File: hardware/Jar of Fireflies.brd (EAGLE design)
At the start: 81.3 x 81.3 mm, 17 parts, among them IC1 ATTINY85, J1 POWER_JACKPTH, J3 M022.54MM_SCREWTERM

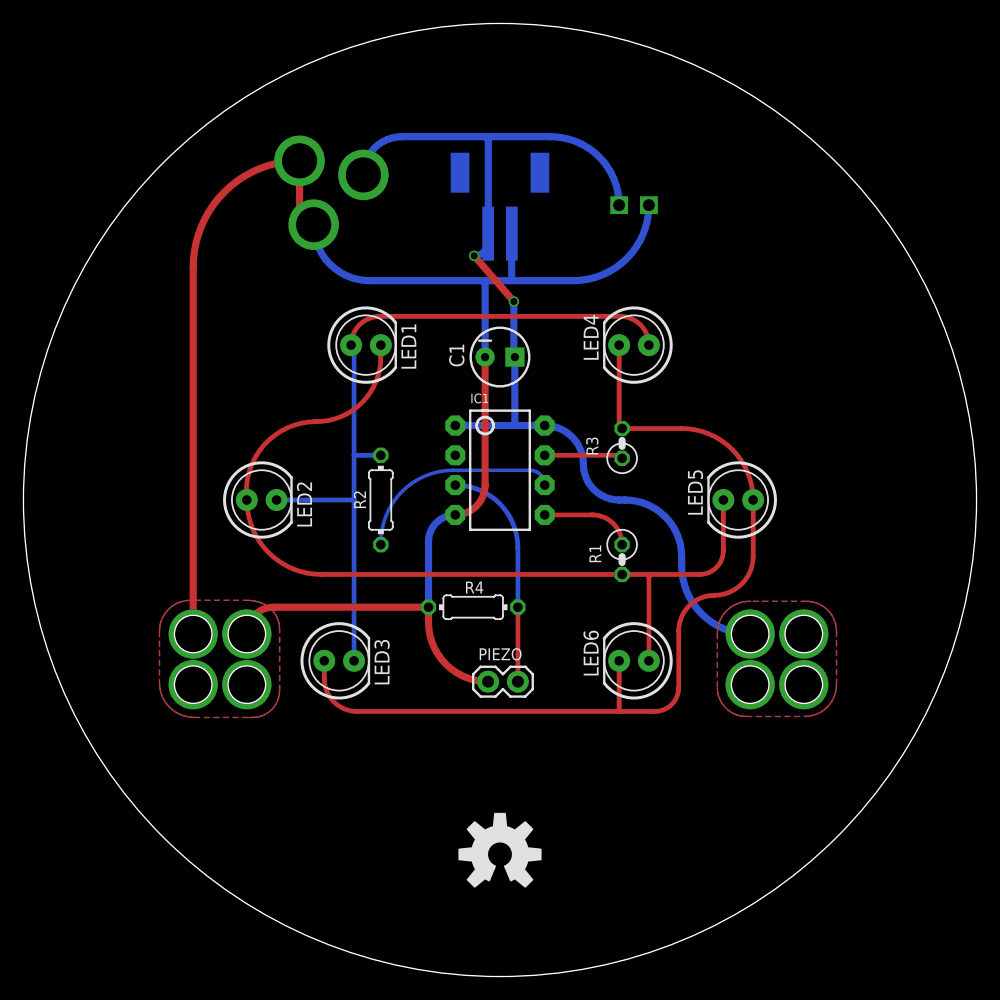
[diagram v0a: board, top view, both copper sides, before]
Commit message: Updating PCB design with ICSP, SMD pads for LEDs, sensor interface, and different power options
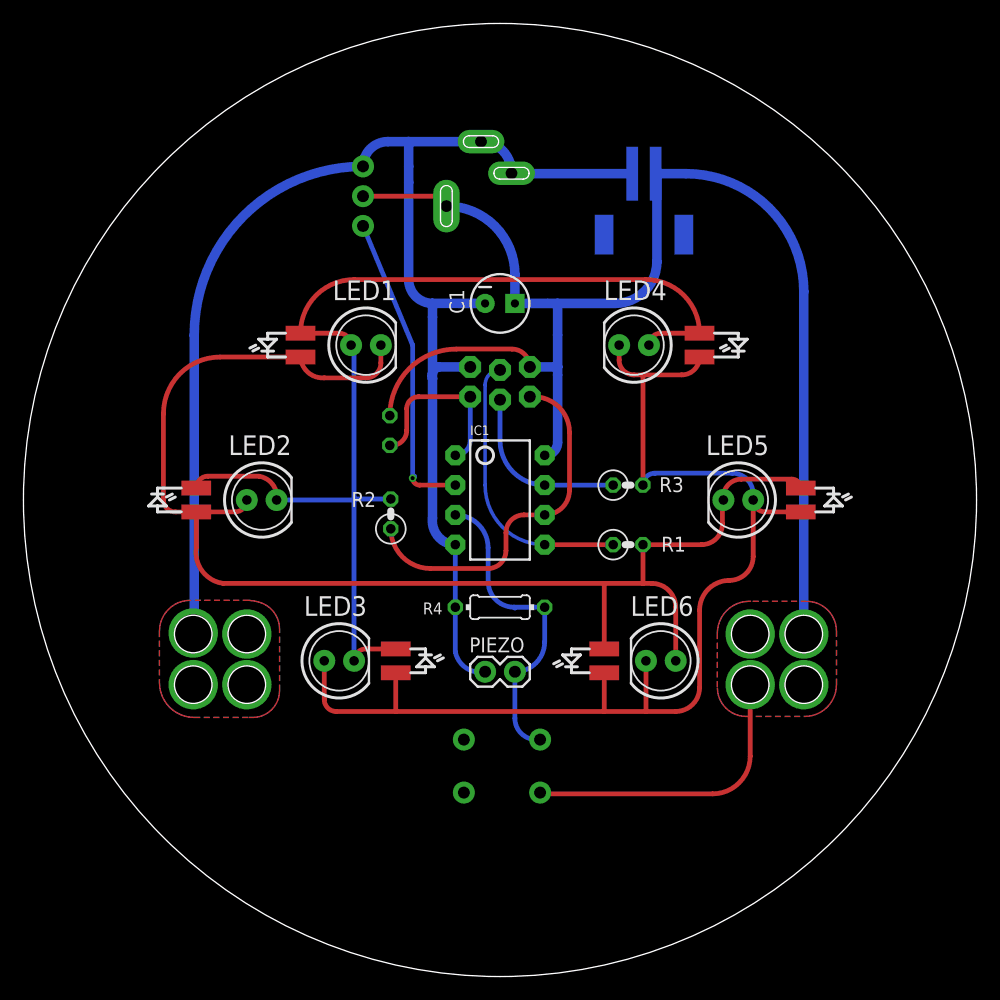
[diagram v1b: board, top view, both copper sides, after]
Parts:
- removed LOGO1: OSHW-LOGOL, SparkFun-Aesthetics:OSHW-LOGO-L
- added J4: ICSP, SparkFun-Connectors:2X3_LOCK
- added PAD1, PAD10, PAD11, PAD12, PAD2, PAD3, PAD4, PAD5, PAD6, PAD7, PAD8, PAD9: (no value), wirepad:SMD1,27-2,54
- added R5: 10k, resistor:0207/2V
- added S1: (no value), SparkFun-Electromechanical:TACTILE-PTH
- J1: value POWER_JACKPTH -> PJ-006A; device SparkFun-Connectors:POWER_JACK_PTH -> PJ-006A:CUI_PJ-006A
- J2: value (none) -> JST
- J3: value M022.54MM_SCREWTERM -> SENSOR; device SparkFun-Connectors:1X02_2.54_SCREWTERM -> SparkFun-Connectors:1X03
- R1, R3: value 150 -> (none)
- R2: value 150 -> (none); device resistor:0204/7 -> resistor:0207/2V
- moved J3 24.4 mm to (29.0, 64.0), turned to 90 degrees
- moved J1 18.2 mm to (36.1, 65.7), turned to 270 degrees
- moved J2 12.5 mm to (52.9, 64.8), turned to 180 degrees
- moved C1 4.57 mm to (40.6, 57.4)
- moved R3 3.59 mm to (51.6, 41.9), turned to 0 degrees
- moved IC1 2.54 mm to (40.6, 40.6)
- moved LED6 2.29 mm to (54.4, 26.9)
- moved R4 2.29 mm to (40.6, 31.5)
- moved R2 1.46 mm to (31.3, 39.5)
- moved R1 1.37 mm to (51.6, 36.8), turned to 0 degrees
- moved PIEZO 0.88 mm to (39.4, 26.0)
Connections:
- removed net N$1: LED1.A, LED2.K, LED3.K, LED4.A, R2.2
- removed net N$3: LED3.A, LED4.K, LED5.A, LED6.K, R3.2
- removed net PORTA: IC1.5, R1.1
- removed net PORTB: IC1.6, R2.1
- removed net PORTC: IC1.7, R3.1
- new net A: LED1.K, LED2.A, LED5.K, LED6.A, PAD1.1, PAD11.1, PAD5.1, PAD9.1, R1.2
- new net B: LED1.A, LED2.K, LED3.K, LED4.A, PAD2.1, PAD3.1, PAD6.1, PAD7.1, R2.2
- new net C: LED3.A, LED4.K, LED5.A, LED6.K, PAD10.1, PAD12.1, PAD4.1, PAD8.1, R3.2
- new net MISO: IC1.6, J4.1, R2.1
- new net MOSI: IC1.5, J4.4, R1.1
- new net RESET: IC1.1, J4.5, R5.1
- new net SCK: IC1.7, J4.3, R3.1
- new net SENSOR: IC1.2, J3.1
- net GND: now also J1.2, J1.3, J3.3, J4.6; no longer J1.GND, J1.GNDBREAK, J3.P2
- net N$2: now also PIEZO.2, R4.2, S1.1; no longer LED1.K, LED2.A, LED5.K, LED6.A, R1.2
- net PIEZO: no longer PIEZO.2, R4.2
- net VCC: now also J1.1, J3.2, J4.2, R5.2, S1.3; no longer IC1.1, J1.PWR, J3.P1
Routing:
- net A: track 0.00 -> 115.7 mm
- net C: track 0.00 -> 99.6 mm
- net B: track 0.00 -> 96.3 mm
- net N$3: track 77.6 -> 0.00 mm
- net N$1: track 63.3 -> 0.00 mm
- net N$2: track 73.6 -> 13.4 mm
- net VCC: track 85.6 -> 141.4 mm, vias 6 -> 4
- net MISO: track 0.00 -> 29.9 mm
- net SENSOR: track 0.00 -> 26.5 mm, vias 0 -> 1
- net MOSI: track 0.00 -> 23.4 mm
- net PORTB: track 17.2 -> 0.00 mm
- net RESET: track 0.00 -> 15.2 mm
- net GND: track 142.2 -> 127.3 mm
- net SCK: track 0.00 -> 14.7 mm
- net PORTA: track 7.66 -> 0.00 mm
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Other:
- board text added: "S"
- board text added: "Silkscreen artwork is on layer 200"
- board text removed: "OSHW"
- board text removed: "REV B"

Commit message: Switching to vertical JST jack
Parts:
- J2: value JST -> (none); device SparkFun-Connectors:JST-2-SMD -> SparkFun-Connectors:JST-2-PTH-VERT
- moved J2 2.19 mm to (51.6, 66.6), turned to 270 degrees
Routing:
- net VCC: track 141.4 -> 129.6 mm, vias 4 -> 5
- net SENSOR: track 26.5 -> 27.4 mm
- net GND: track 127.3 -> 128.1 mm
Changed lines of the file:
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@@
 <attribute name="NAME" x="54.22064375" y="41.317240625" size="1.27" layer="25" font="vector" ratio="12"/>
-</element>
-<element name="J2" library="SparkFun-Connectors" package="JST-2-SMD" value="JST" x="52.916734375" y="64.769975" smashed="yes" rot="MR180">
-<attribute name="PROD_ID" value="CONN-08352" x="52.916734375" y="64.769975" size="1.778" layer="28" rot="MR180" display="off"/>
 </element>
 <element name="C1" library="SparkFun-Capacitors" package="CPOL-RADIAL-10UF-25V" value="10uF" x="40.64" y="57.404353125" smashed="yes">
@@
 <attribute name="STANDARD" value="Manufacturer recommendations" x="36.069803125" y="65.704625" size="1.778" layer="28" rot="MR270" display="off"/>
 </element>
+<element name="J2" library="SparkFun-Connectors" package="JST-2-PTH-VERT" value="" x="51.64924375" y="66.551328125" rot="MR270"/>
 </elements>
 <signals>
@@
 <contactref element="PIEZO" pad="1"/>
 <contactref element="R4" pad="1"/>
-<contactref element="J2" pad="1"/>
 <contactref element="C1" pad="2"/>
 <via x="19.05" y="29.21" extent="1-16" drill="3.2"/>
@@
 <wire x1="41.619803125" y1="68.604625" x2="41.619803125" y2="68.504625" width="0.8128" layer="16"/>
 <wire x1="41.619803125" y1="68.504625" x2="41.654453125" y2="68.469975" width="0.8128" layer="16" curve="90"/>
-<wire x1="41.654453125" y1="68.469975" x2="51.916734375" y2="68.469975" width="0.8128" layer="16"/>
 <wire x1="32.852309375" y1="69.091453125" x2="32.852309375" y2="69.091453125" width="0.8128" layer="16" curve="90"/>
 <wire x1="32.852309375" y1="69.091453125" x2="32.852309375" y2="67.73671875" width="0.8128" layer="16"/>
@@
 <wire x1="14.56339375" y1="54.69715" x2="28.95745" y2="69.09120625" width="0.8128" layer="16" curve="-90"/>
 <wire x1="14.56339375" y1="29.38028125" x2="14.56339375" y2="54.69715" width="0.8128" layer="16"/>
+<contactref element="J2" pad="1"/>
+<wire x1="41.619803125" y1="68.504625" x2="51.245946875" y2="68.504625" width="0.8128" layer="16"/>
+<wire x1="51.245946875" y1="68.504625" x2="52.19924375" y2="67.551328125" width="0.8128" layer="16" curve="-90"/>
 </signal>
 <signal name="MISO">
@@
 <signal name="VCC">
 <contactref element="IC1" pad="8"/>
-<contactref element="J2" pad="2"/>
 <contactref element="C1" pad="1"/>
 <via x="61.976" y="29.21" extent="1-16" drill="3.2"/>
-<via x="66.548" y="29.21" extent="1-16" drill="3.2"/>
 <via x="66.548" y="24.892" extent="1-16" drill="3.2"/>
 <via x="61.976" y="24.892" extent="1-16" drill="3.2"/>
@@
 <vertex x="61.631171875" y="22.180446875"/>
 </polygon>
-<wire x1="66.548" y1="58.42" x2="66.548" y2="29.21" width="0.8128" layer="16"/>
 <contactref element="S1" pad="3"/>
-<wire x1="53.916734375" y1="68.469975" x2="56.498025" y2="68.469975" width="0.8128" layer="16"/>
-<wire x1="56.498025" y1="68.469975" x2="66.548" y2="58.42" width="0.8128" layer="16" curve="-90"/>
 <wire x1="61.976" y1="24.892" x2="61.976" y2="18.79384375" width="0.4064" layer="1"/>
 <wire x1="61.976" y1="18.79384375" x2="58.761603125" y2="15.579446875" width="0.4064" layer="1" curve="-90"/>
@@
 <wire x1="44.1698375" y1="15.579446875" x2="44.060540625" y2="15.68874375" width="0.4064" layer="1" curve="-90"/>
 <contactref element="J4" pad="2"/>
-<wire x1="44.45" y1="44.45" x2="45.55294375" y2="45.55294375" width="0.8128" layer="16" curve="90"/>
-<wire x1="45.55294375" y1="54.69694375" x2="45.55294375" y2="51.98793125" width="0.8128" layer="16"/>
-<wire x1="45.55294375" y1="51.310565625" x2="45.55294375" y2="45.55294375" width="0.8128" layer="16"/>
 <wire x1="43.182290625" y1="51.9878" x2="43.182421875" y2="51.98793125" width="0.8128" layer="16" curve="-90"/>
 <contactref element="R5" pad="2"/>
@@
 <wire x1="36.91501875" y1="53.512009375" x2="41.657953125" y2="53.512009375" width="0.4064" layer="1"/>
 <wire x1="41.657953125" y1="53.512009375" x2="43.182159375" y2="51.987803125" width="0.4064" layer="1" curve="-90"/>
-<wire x1="41.91" y1="57.404353125" x2="44.706234375" y2="57.404353125" width="0.8128" layer="16"/>
-<wire x1="44.706234375" y1="57.404353125" x2="45.55294375" y2="57.404353125" width="0.8128" layer="16"/>
-<wire x1="45.55294375" y1="57.404353125" x2="45.55294375" y2="54.69694375" width="0.8128" layer="16"/>
 <contactref element="J1" pad="1"/>
-<wire x1="45.55294375" y1="51.98793125" x2="45.55294375" y2="51.310565625" width="0.8128" layer="16"/>
-<wire x1="43.182159375" y1="51.987803125" x2="45.552815625" y2="51.987803125" width="0.8128" layer="16"/>
-<wire x1="45.552815625" y1="51.987803125" x2="45.55294375" y2="51.98793125" width="0.8128" layer="16"/>
-<wire x1="45.55294375" y1="57.404353125" x2="50.461340625" y2="57.404353125" width="0.8128" layer="16"/>
-<wire x1="50.461340625" y1="57.404353125" x2="54.020034375" y2="60.963046875" width="0.8128" layer="16" curve="90"/>
-<wire x1="54.020034375" y1="60.963046875" x2="54.020034375" y2="68.366675" width="0.8128" layer="16"/>
-<wire x1="54.020034375" y1="68.366675" x2="53.916734375" y2="68.469975" width="0.8128" layer="16" curve="90"/>
 <contactref element="J3" pad="2"/>
-<wire x1="36.069803125" y1="65.704625" x2="41.91" y2="59.864428125" width="0.8128" layer="16" curve="-90"/>
-<wire x1="41.91" y1="59.864428125" x2="41.91" y2="57.404353125" width="0.8128" layer="16"/>
 <wire x1="28.95745" y1="66.55120625" x2="35.223221875" y2="66.55120625" width="0.4064" layer="1"/>
 <wire x1="35.223221875" y1="66.55120625" x2="36.069803125" y2="65.704625" width="0.4064" layer="1" curve="-90"/>
+<contactref element="J2" pad="2"/>
+<via x="66.548228125" y="29.21" extent="1-16" drill="3.2"/>
+<wire x1="66.548228125" y1="29.21" x2="66.548228125" y2="48.916953125" width="0.8128" layer="16"/>
+<wire x1="36.069803125" y1="65.704625" x2="41.65808125" y2="65.704625" width="0.8128" layer="16"/>
+<wire x1="41.91" y1="57.404353125" x2="41.91" y2="65.45270625" width="0.8128" layer="16"/>
+<wire x1="41.91" y1="65.45270625" x2="41.65808125" y2="65.704625" width="0.8128" layer="16" curve="90"/>
+<wire x1="43.182159375" y1="51.987803125" x2="43.182159375" y2="56.13219375" width="0.8128" layer="16"/>
+<wire x1="43.182159375" y1="56.13219375" x2="41.91" y2="57.404353125" width="0.8128" layer="16" curve="90"/>
+<wire x1="44.45" y1="44.45" x2="45.55294375" y2="45.55294375" width="0.8128" layer="16" curve="90"/>
+<wire x1="45.55294375" y1="49.61701875" x2="43.182159375" y2="51.987803125" width="0.8128" layer="16" curve="90"/>
+<wire x1="45.55294375" y1="45.55294375" x2="45.55294375" y2="49.61701875" width="0.8128" layer="16"/>
+<via x="66.548228125" y="48.916953125" extent="1-16" drill="0.35"/>
+<wire x1="41.65808125" y1="65.704625" x2="52.045946875" y2="65.704625" width="0.8128" layer="16"/>
+<wire x1="52.045946875" y1="65.704625" x2="52.19924375" y2="65.551328125" width="0.8128" layer="16" curve="-90"/>
+<wire x1="66.548228125" y1="48.916953125" x2="66.548228125" y2="51.20234375" width="0.8128" layer="16"/>
+<wire x1="66.548228125" y1="51.20234375" x2="52.19924375" y2="65.551328125" width="0.8128" layer="16" curve="90"/>
 <wire x1="43.182159375" y1="51.987803125" x2="43.182290625" y2="51.9878" width="0" layer="19" extent="16-16"/>
 </signal>
@@
 <wire x1="33.785784375" y1="41.91" x2="33.19099375" y2="42.504790625" width="0.4064" layer="1" curve="-90"/>
 <wire x1="33.19099375" y1="42.504790625" x2="33.360334375" y2="42.67413125" width="0.4064" layer="16" curve="90"/>
-<wire x1="33.19099375" y1="42.504790625" x2="33.19099375" y2="53.85069375" width="0.4064" layer="16"/>
-<wire x1="33.19099375" y1="53.85069375" x2="28.95745" y2="64.01120625" width="0.4064" layer="16"/>
+<wire x1="33.19099375" y1="55.036084375" x2="31.497575" y2="56.729503125" width="0.4064" layer="16" curve="90"/>
+<wire x1="31.497575" y1="56.729503125" x2="28.95745" y2="59.269628125" width="0.4064" layer="16" curve="-90"/>
+<wire x1="28.95745" y1="59.269628125" x2="28.95745" y2="64.01120625" width="0.4064" layer="16"/>
+<wire x1="33.19099375" y1="42.504790625" x2="33.19099375" y2="55.036084375" width="0.4064" layer="16"/>
 </signal>
 <signal name="N$2">
